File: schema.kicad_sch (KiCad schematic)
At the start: 74 parts, among them J1 USB_C_Receptacle_PowerOnly_6P, J2 Screw_Terminal_01x04, J4 PINHD_1x3_Female, J5 HW-084, J6 2x3, J7 1x2, SW1 RESET, U1 ATmega328/ATmega328P, U2 TPIC6B595N/TPIC6595N, U3 TPIC6B595N/TPIC6595N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

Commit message: Preventívne uloženie na github.
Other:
- note added: "SPI rozhranie by sa dalo použiť pri hardvérovom posúvaní bitov do registrov, čo by zvýšilo efektivitu, ale bolo by treba previazať: SERIN (PB4) -> MOSI (PB3) SRCK (PB0) -> SCK (PB5) Na pine PB3 je pripojená modrá časť indikačnej RGB ledky, ale keďže PB3 používa timer2 zatiaľ čo ostatné farby (PB1 a PB2) používajú timer1, PWM na tomto pine riešime aj tak softvérovo a môže byť premiestnený."

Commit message: Opravy v schéme. Úpravy a optimalizácie firmvéru.
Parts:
- added R18, R25: 620R, Resistor_THT:R_Axial_DIN0207_L6.3mm_D2.5mm_P7.62mm_Horizontal, symbol PCM_SL_Resistors:Resistor
- C1, C2: value 68pF±5% -> 33pF±5%
- Y1: Url (none) -> https://www.tme.eu/en/details/16.00m-hc49-s/tht-quartz-crys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
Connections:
- net HBTN: now also R18.2; no longer TLACIDLO1.2
- net VBTN: now also R25.2; no longer TLACIDLO2.2
- new net: R25.1, TLACIDLO2.2
- new net: R18.1, TLACIDLO1.2
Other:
- moved on the sheet: TLACIDLO1, TLACIDLO2

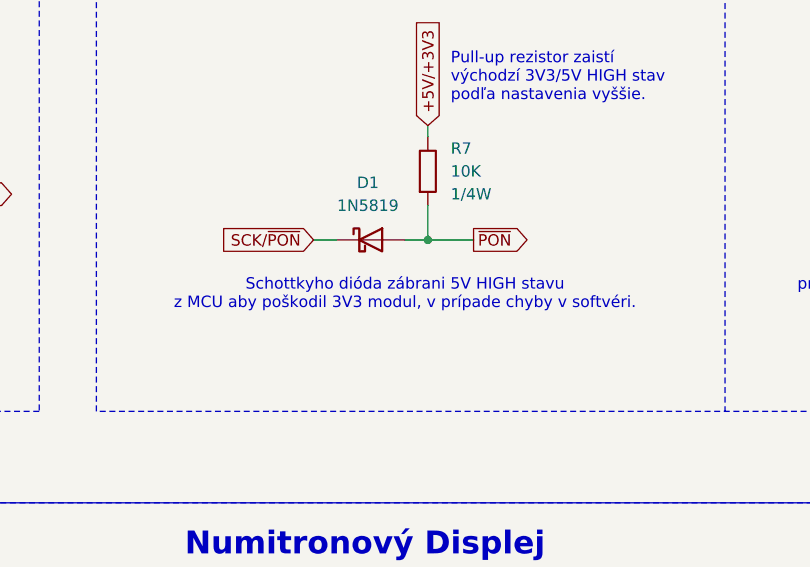
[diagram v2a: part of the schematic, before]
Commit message: Dalsie masivne zmeny. Pridané casovace, aj ked zatial este moc nefunguju.
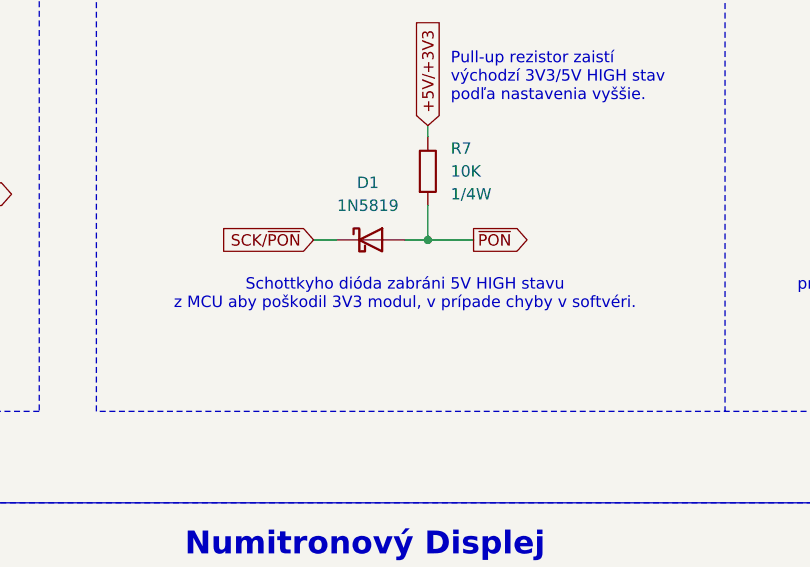
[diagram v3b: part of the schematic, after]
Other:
- note added: "Schottkyho dióda zabráni 5V HIGH stavu z MCU aby poškodil 3V3 modul, v prípade chyby v softvéri."
- note removed: "Schottkyho dióda zábrani 5V HIGH stavu z MCU aby poškodil 3V3 modul, v prípade chyby v softvéri."
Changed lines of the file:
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@@
 		)
 	)
-	(text "Schottkyho dióda zábrani 5V HIGH stavu\nz MCU aby poškodil 3V3 modul, v prípade chyby v softvéri."
+	(text "Schottkyho dióda zabráni 5V HIGH stavu\nz MCU aby poškodil 3V3 modul, v prípade chyby v softvéri."
 		(exclude_from_sim no)
 		(at 417.83 116.586 0)

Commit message: Upravený návrh dosky.
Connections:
- net HBTN: no longer C6.2
- net VBTN: no longer C7.2
- net at R25.1, TLACIDLO2.2: now also C7.2
- net at R18.1, TLACIDLO1.2: now also C6.2
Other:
- moved on the sheet: C6, C7
